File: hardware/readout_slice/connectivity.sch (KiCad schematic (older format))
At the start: 17 parts

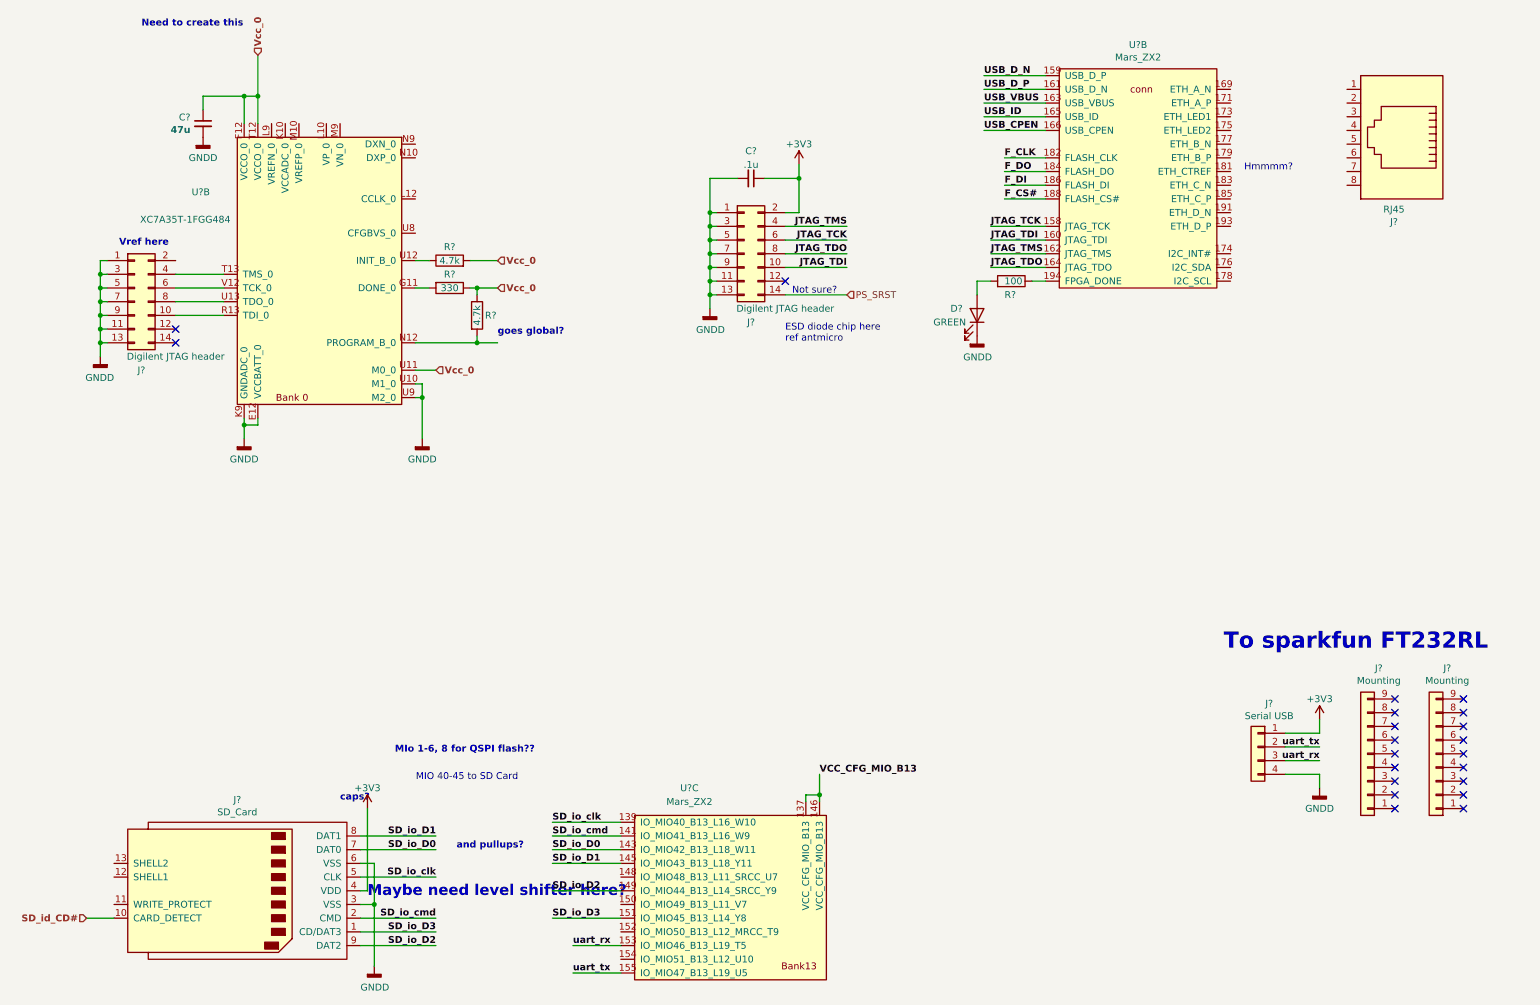
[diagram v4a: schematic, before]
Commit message: readout_slice is more ordered now
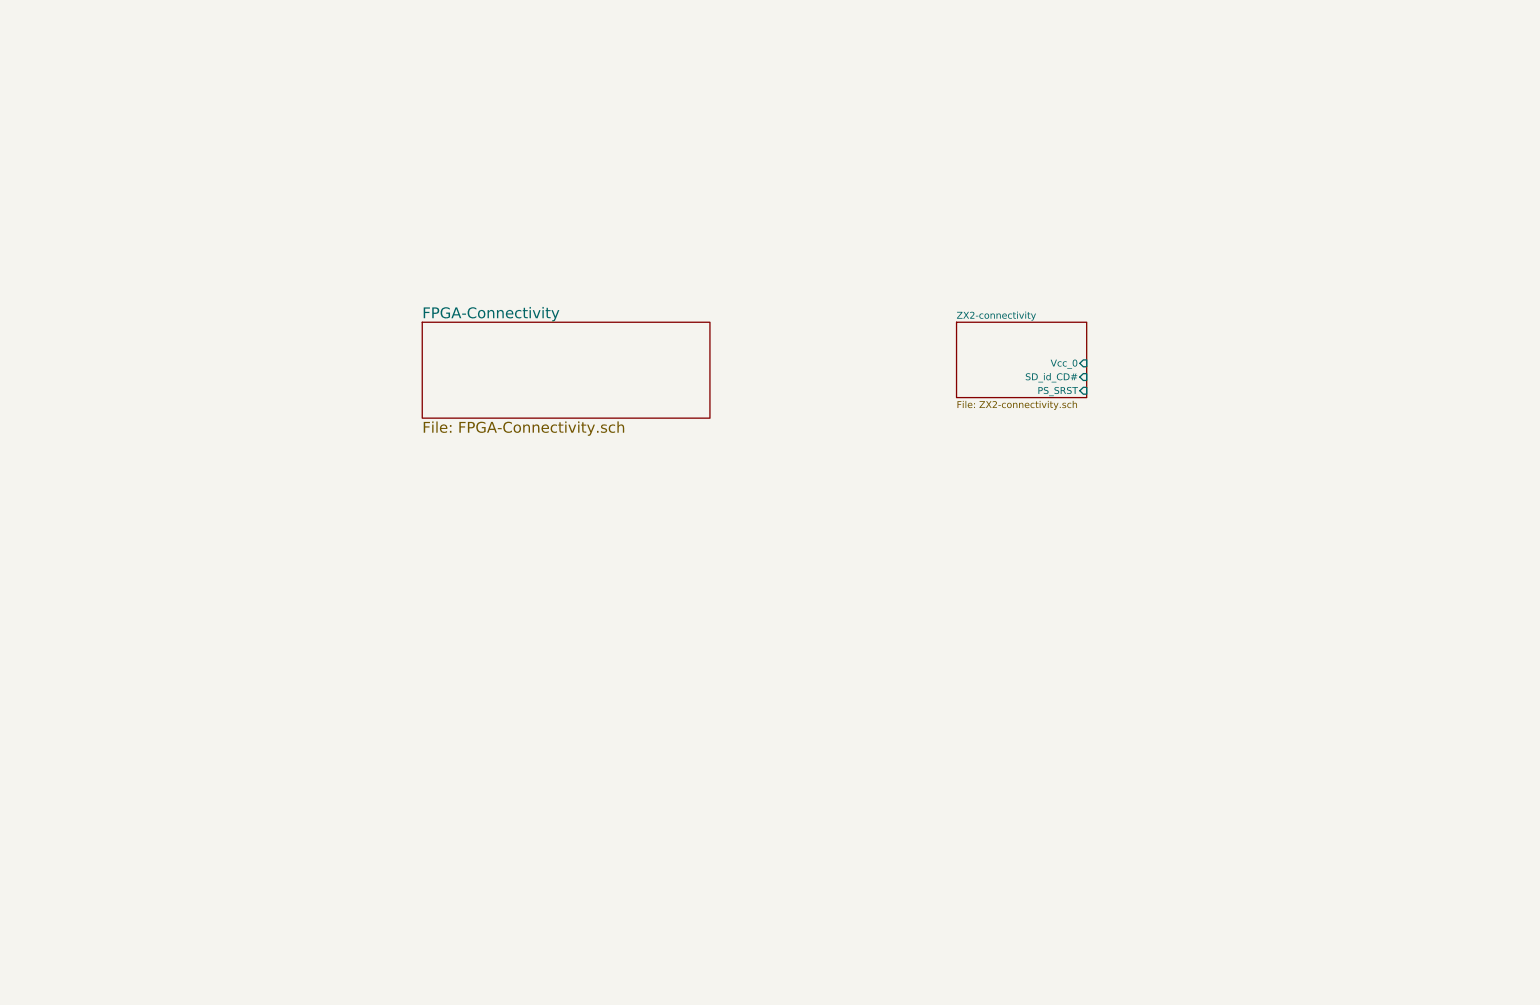
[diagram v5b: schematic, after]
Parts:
- removed C?: .1u, symbol Device:C_Small
- removed C?: 47u, symbol Device:C_Small
- removed D?: GREEN, symbol Device:LED
- removed J?: Serial USB, symbol Connector_Generic:Conn_01x04
- removed J? (x2): Mounting, symbol Connector_Generic:Conn_01x09
- removed J? (x2): Digilent JTAG header, readout_slice:87832-1420, symbol Connector_Generic:Conn_02x07_Odd_Even
- removed J?: RJ45, symbol Connector:RJ45
- removed J?: SD_Card, symbol Connector:SD_Card
- removed R?: 100, symbol Device:R
- removed R?: 330, symbol Device:R
- removed R? (x2): 4.7k, symbol Device:R
- removed U? (x2): Mars_ZX2, symbol readout:Mars_ZX2
- removed U?: XC7A35T-1FGG484, symbol readout:XC7A35T-1FGG484
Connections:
- no-connect marks 21 -> 0
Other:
- note removed: "ESD diode chip here\nref antmicro"
- note removed: "Hmmmm?"
- note removed: "MIO 40-45 to SD Card"
- note removed: "MIo 1-6, 8 for QSPI flash??\n"
- note removed: "Maybe need level shifter here?"
- note removed: "Need to create this"
- note removed: "Not sure?"
- note removed: "To sparkfun FT232RL"
- note removed: "Vref here"
- note removed: "and pullups?\n"
- note removed: "caps?"
- note removed: "goes global?"
